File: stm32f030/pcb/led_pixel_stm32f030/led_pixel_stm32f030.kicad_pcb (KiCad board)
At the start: 2 copper layers, 50 x 50 mm, 52 parts, among them CON1 10PIN_JTAG_SWD, J1 Screw_Terminal_1x02, J2 CONN_01X10, J3 CONN_01X10, Q1 BC107, U1 STM32F030F4Px, U2 SN75176, U3 1117-3.3, U4 PT4115, U5 PT4115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

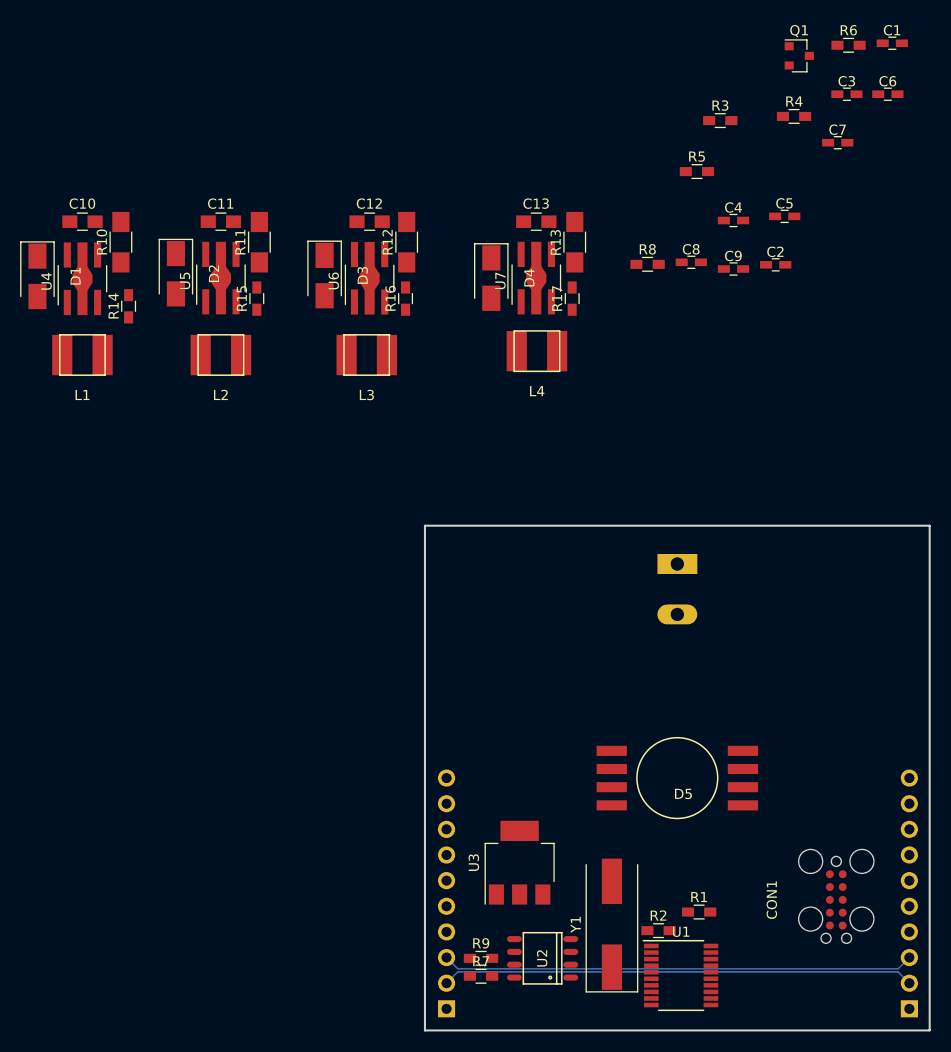
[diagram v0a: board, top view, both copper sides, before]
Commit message: made a first layout draft...
well okay, wouldn´t call it layout yet ;)

- next step make it look like a Layout XD
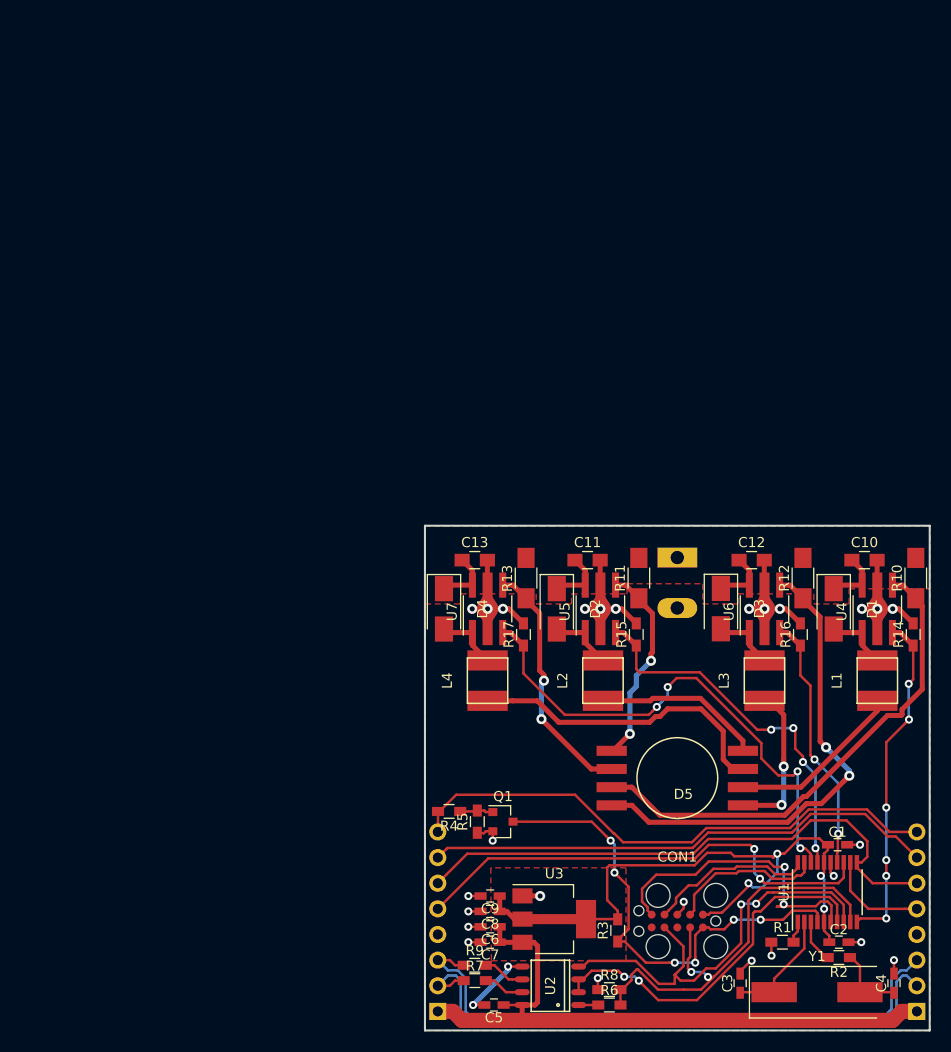
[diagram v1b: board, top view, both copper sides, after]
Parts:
- J2, J3: value CONN_01X10 -> CONN_01X08; footprint Pin_Headers:Pin_Header_Straight_1x10_Pitch2.54mm -> Pin_Headers:Pin_Header_Straight_1x08_Pitch2.54mm
- moved R6 98.0 mm to (143.3, 122.5)
- moved C6 91.4 mm to (131.5, 114.7), turned to 180 degrees
- moved C3 88.7 mm to (156.2, 120.3), turned to 90 degrees
- moved C7 86.4 mm to (131.5, 116.3), turned to 180 degrees
- moved D1 85.5 mm to (165.5, 83.2)
- moved R10 85.5 mm to (173.6, 80.2)
- moved U4 85.3 mm to (169.8, 83.2)
- moved L1 85.1 mm to (169.8, 90.3), turned to 90 degrees
- moved C10 84.4 mm to (168.5, 78.4)
- moved R14 84.2 mm to (173.4, 85.8)
- moved C5 83.3 mm to (131.8, 122.5), turned to 180 degrees
- moved Q1 81.3 mm to (132.7, 104.3)
- moved R3 80.9 mm to (144.1, 115.1), turned to 90 degrees
- moved C1 79.6 mm to (165.9, 106.6)
- moved C4 77.2 mm to (171.5, 120.3), turned to 90 degrees
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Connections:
- J2 pad 1: GND -> +5V
- J2 pad 5: /backplane/RESERVED -> /SPI_MOSI
- J2 pad 6: +5V -> /SPI_CLK
- J2 pad 7: /SPI_CLK -> /backplane/DAISY_R_TO_L
- J3 pad 1: GND -> +5V
- J3 pad 5: /backplane/RESERVED -> /SPI_MISO
- J3 pad 6: +5V -> /SPI_CLK
- J3 pad 7: /SPI_CLK -> /backplane/DAISY_R_TO_L
- U1 pad 14: /PWM_LED_W -> /PWM_LED_B
- U1 pad 18: /PWM_LED_B -> /PWM_LED_W
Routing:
- net GND: track 0.00 -> 81.9 mm, vias 0 -> 28
- net +3V3: track 0.00 -> 64.6 mm, vias 0 -> 4
- net +5V: track 0.00 -> 64.3 mm
- net /SPI_CLK: track 0.00 -> 55.9 mm
- net /RESET_IN: track 0.00 -> 54.4 mm
- net /PWM_LED_W: track 0.00 -> 51.1 mm, vias 0 -> 4
- net /backplane/DAISY_R_TO_L: track 0.00 -> 51.0 mm
- net /rgbw_led_driver/LED_R_A: track 0.00 -> 49.5 mm
- net /rgbw_led_driver/LED_B_A: track 0.00 -> 48.6 mm, vias 0 -> 2
- net /SPI_MOSI: track 0.00 -> 47.5 mm, vias 0 -> 2
- net /#RESET: track 0.00 -> 47.1 mm, vias 0 -> 6
- net /RS485_TX: track 0.00 -> 42.5 mm, vias 0 -> 2
- net /RS485_RX: track 0.00 -> 42.3 mm, vias 0 -> 2
- net /PWM_LED_G: track 0.00 -> 37.3 mm, vias 0 -> 4
- net /RS485_DE: track 0.00 -> 36.5 mm, vias 0 -> 2
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- added copper zone on F.Cu, net +3V3
- added copper zone on B.Cu, net GND
- added copper zone on F.Cu, net GND
- added copper zone on F.Cu, net VCC

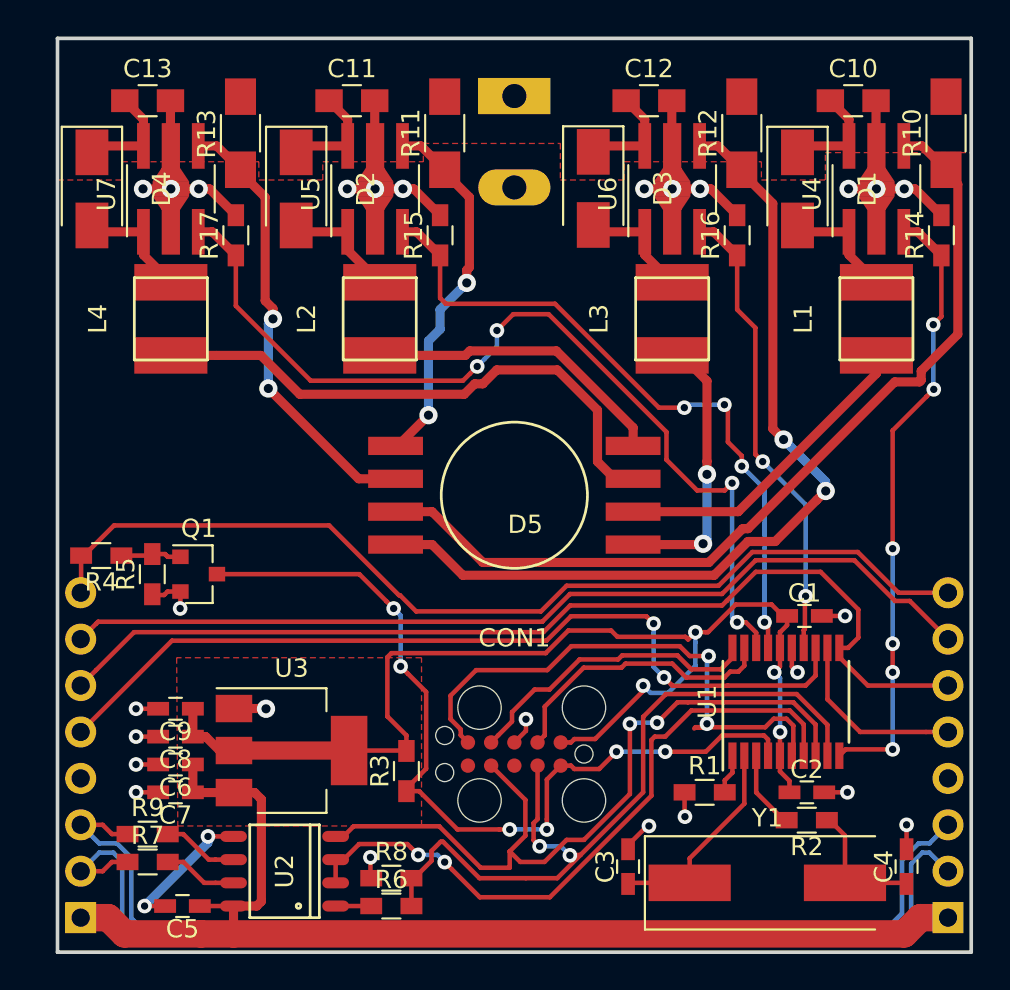
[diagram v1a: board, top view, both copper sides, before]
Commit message: added mounting holes
added a lot of capacitors (there was some room left ;) )

layout nearly finished
logos are missing ;)
not much work left I think
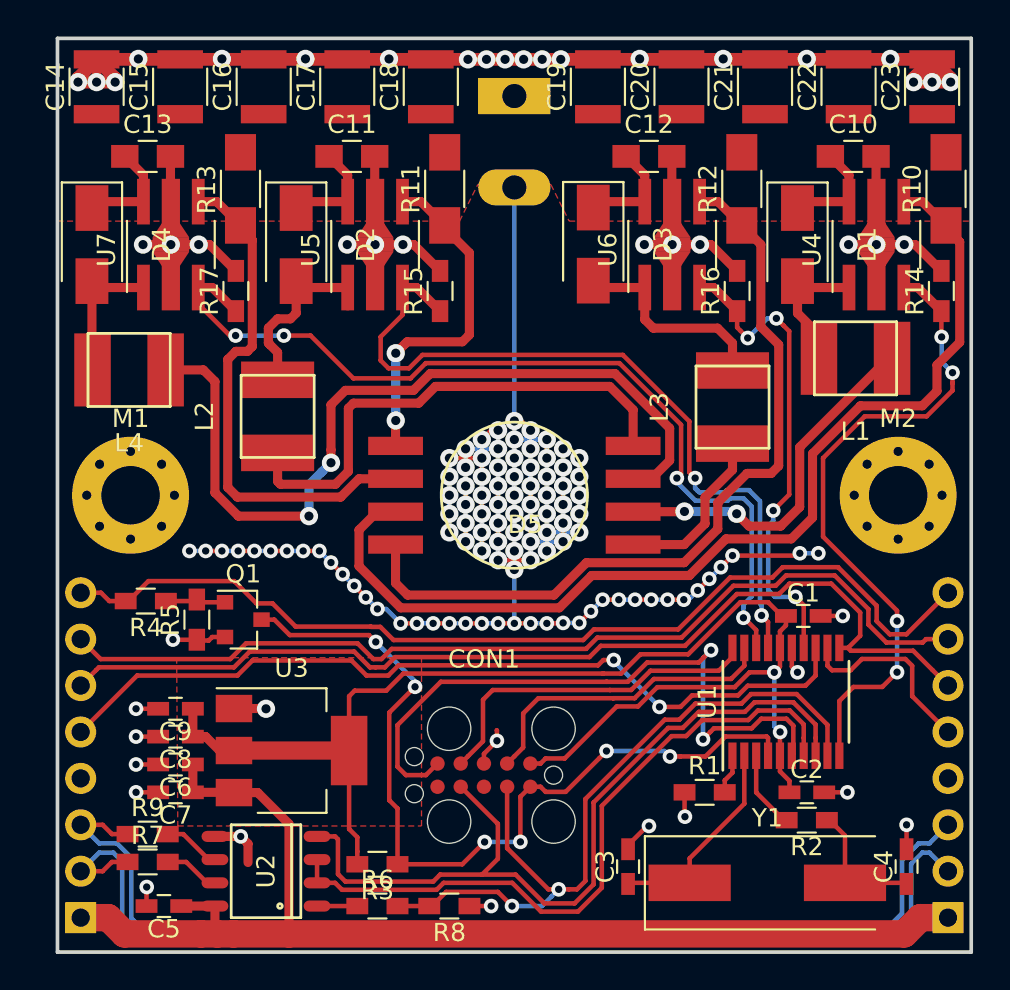
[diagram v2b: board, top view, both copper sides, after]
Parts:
- added C14: 10u 50V, Capacitors_SMD:C_1210, F.Cu at (127.1, 77.6)
- added C15: 10u 50V, Capacitors_SMD:C_1210, F.Cu at (131.7, 77.6)
- added C16: 10u 50V, Capacitors_SMD:C_1210, F.Cu at (136.3, 77.6)
- added C17: 10u 50V, Capacitors_SMD:C_1210, F.Cu at (140.9, 77.6)
- added C18: 10u 50V, Capacitors_SMD:C_1210, F.Cu at (145.4, 77.6)
- added C19: 10u 50V, Capacitors_SMD:C_1210, F.Cu at (154.6, 77.6)
- added C20: 10u 50V, Capacitors_SMD:C_1210, F.Cu at (159.1, 77.6)
- added C21: 10u 50V, Capacitors_SMD:C_1210, F.Cu at (163.7, 77.6)
- added C22: 10u 50V, Capacitors_SMD:C_1210, F.Cu at (168.3, 77.6)
- added C23: 10u 50V, Capacitors_SMD:C_1210, F.Cu at (172.9, 77.6)
- added M1: mounting hole, Mounting_Holes:MountingHole_3.2mm_M3_Pad_Via, F.Cu at (129.0, 100.0)
- added M2: mounting hole, Mounting_Holes:MountingHole_3.2mm_M3_Pad_Via, F.Cu at (171.0, 100.0)
- moved L2 7.73 mm to (137.0, 95.7)
- moved L3 5.85 mm to (161.9, 95.2)
- moved R3 5.34 mm to (142.5, 120.2), turned to 180 degrees
- moved L4 3.61 mm to (128.9, 93.1), turned to 180 degrees
- moved R8 3.52 mm to (146.4, 122.5), turned to 180 degrees
- moved Q1 3.48 mm to (135.2, 106.8)
- moved R4 3.48 mm to (129.8, 105.8)
- moved R5 3.48 mm to (132.6, 106.8)
- moved C10 3.05 mm to (168.5, 81.5)
- moved C11 3.05 mm to (141.1, 81.5)
- moved C12 3.05 mm to (157.4, 81.5)
- moved C13 3.05 mm to (129.9, 81.5)
- moved D1 3.05 mm to (165.5, 86.3)
- moved D2 3.05 mm to (138.1, 86.3)
- moved D3 3.05 mm to (154.3, 86.3)
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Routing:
- net GND: track 81.9 -> 262.3 mm, vias 28 -> 148
- net /rgbw_led_driver/LED_W_K: track 30.8 -> 47.0 mm, vias 0 -> 2
- net /rgbw_led_driver/LED_G_K: track 16.7 -> 27.8 mm
- net /rgbw_led_driver/LED_R_A: track 49.5 -> 57.6 mm
- net +3V3: track 64.6 -> 71.8 mm, vias 4 -> 2
- net /rgbw_led_driver/LED_B_K: track 15.5 -> 9.41 mm, vias 2 -> 0
- net Net-(D3-Pad2): track 6.36 -> 12.5 mm
- net /TESTMODE: track 30.4 -> 36.1 mm
- net /PWM_LED_G: track 37.3 -> 41.9 mm, vias 4 -> 2
- net /rgbw_led_driver/LED_B_A: track 48.6 -> 44.1 mm, vias 2 -> 0
- net Net-(D2-Pad2): track 6.45 -> 10.6 mm
- net /rgbw_led_driver/LED_W_A: track 25.7 -> 29.2 mm, vias 2 -> 0
- net /RS485_TX: track 42.5 -> 45.6 mm, vias 2 -> 0
- net /SWCLK: track 16.6 -> 19.1 mm
- net /PWM_LED_R: track 33.8 -> 36.2 mm, vias 6 -> 4
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
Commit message: finished layout for stm32f0 version
the silkscreen has to be fixed...
documentation and production data has to be generated
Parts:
- added G***: LOGO, proz_logo:Shimatta_SolderMask, B.Cu at (161.5, 120.8)
- added REF**: KiCAD Logo, Symbols:Symbol_KiCAD-Logo_CopperAndSilkScreenTop, B.Cu at (136.8, 115.2)
- added REF***: ESD-Logo_8.9x8mm_SilkScreen, Symbols:ESD-Logo_8.9x8mm_SilkScreen, B.Cu at (169.8, 81.2)
- added REF***: WEEE-Logo_4.2x6mm_SilkScreen, Symbols:WEEE-Logo_4.2x6mm_SilkScreen, B.Cu at (129.2, 81.7)
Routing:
- net /#RESET: track 46.7 -> 52.9 mm
- net GND: track 262.3 -> 264.3 mm, vias 148 -> 149
- net /RS485_TX: track 45.6 -> 47.4 mm
- net /RS485_RX: track 41.2 -> 39.8 mm
- net /rgbw_led_driver/LED_B_A: track 44.1 -> 43.2 mm
- net /rgbw_led_driver/LED_R_A: track 57.6 -> 58.4 mm
- net /rgbw_led_driver/LED_R_K: track 20.2 -> 21.0 mm
- net /backplane/DAISY_R_TO_L: track 52.6 -> 51.9 mm
- net /SPI_CLK: track 55.3 -> 54.6 mm
- net /RS485_DE: track 38.1 -> 37.5 mm
- net /PWM_LED_R: track 36.2 -> 36.7 mm
- net /PWM_LED_W: track 49.6 -> 50.1 mm
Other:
- board text added: "05/2017"

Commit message: hopefully finished everything
generated documentation and gerber files
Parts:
- moved G*** 33.5 mm to (150.0, 89.3)
- moved REF** 0.89 mm to (136.8, 116.1)
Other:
- board text added: "+5V"
- board text added: "GND"
- board text added: "RS485_N"
- board text added: "RS485_P"
- board text added: "daisy clk"
- board text added: "daisy in"
- board text added: "daisy out"
- board text added: "daisy rtn"
- board text added: "reset"

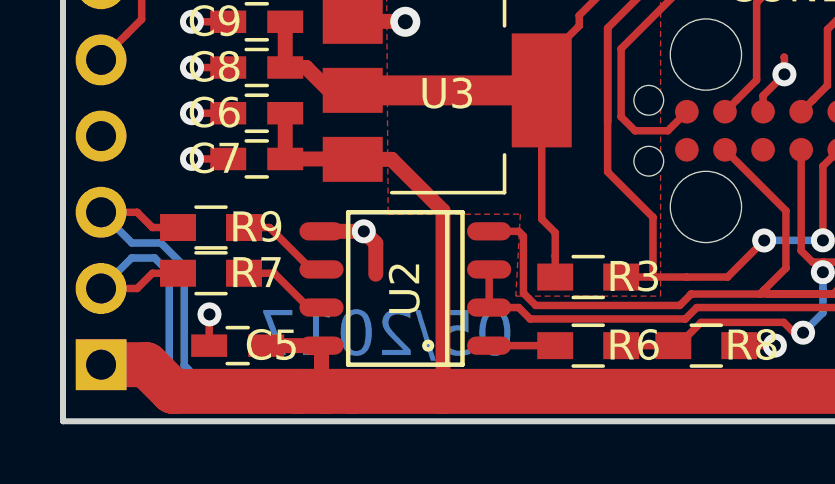
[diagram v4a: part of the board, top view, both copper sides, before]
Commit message: added pcb number and revision
re generated all docu and gerber data
- ordered this one as rev 1.0
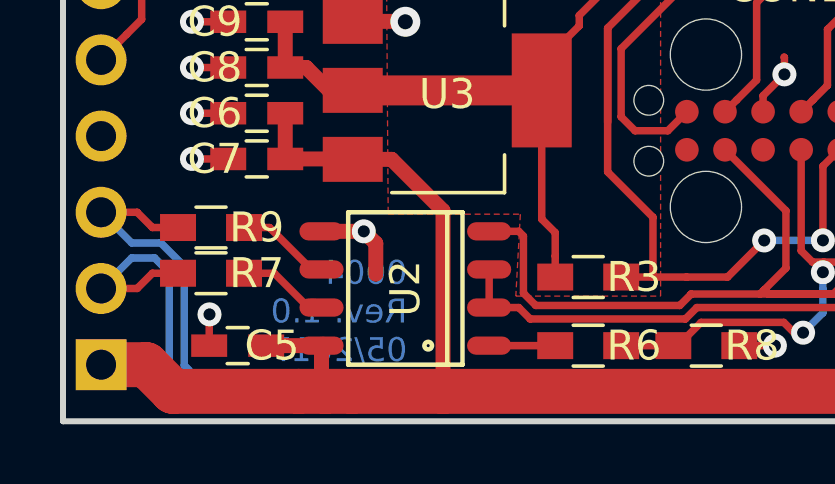
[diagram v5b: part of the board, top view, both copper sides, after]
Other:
- board text added: "0004 Rev: 1.0 05/2017"
- board text removed: "05/2017"
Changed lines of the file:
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@@
-(kicad_pcb (version 20170123) (host pcbnew "(2017-05-08 revision d4e41c4f9)-makepkg")
+(kicad_pcb (version 20170123) (host pcbnew "(2017-05-12 revision b823d0b78)-makepkg")
   (general
     (links 163)
@@
   )
   (page A4)
+  (title_block
+    (title led_pixel_stm32f030)
+    (date 2017-05-13)
+    (rev 1.0)
+    (company shimatta)
+  )
   (layers
     (0 F.Cu signal)
@@
     (visible_elements 7FFFFFFF)
     (pcbplotparams
-      (layerselection 0x000fc_ffffffff)
+      (layerselection 0x010fc_ffffffff)
       (usegerberextensions true)
       (excludeedgelayer false)
@@
       (outputformat 4)
       (mirror false)
-      (drillshape 2)
+      (drillshape 0)
       (scaleselection 1)
       (outputdirectory doc/))
@@
     (effects (font (size 1.5 1.5) (thickness 0.3)) (justify mirror))
   )
-  (gr_text 05/2017 (at 135.776 122.098) (layer B.Cu)
-    (effects (font (size 1.5 1.5) (thickness 0.3)) (justify mirror))
+  (gr_text "0004\nRev: 1.0\n05/2017" (at 136.4745 121.336) (layer B.Cu)
+    (effects (font (size 0.8 0.8) (thickness 0.2)) (justify left mirror))
   )
   (gr_line (start 125 125) (end 125 75) (layer Edge.Cuts) (width 0.2))

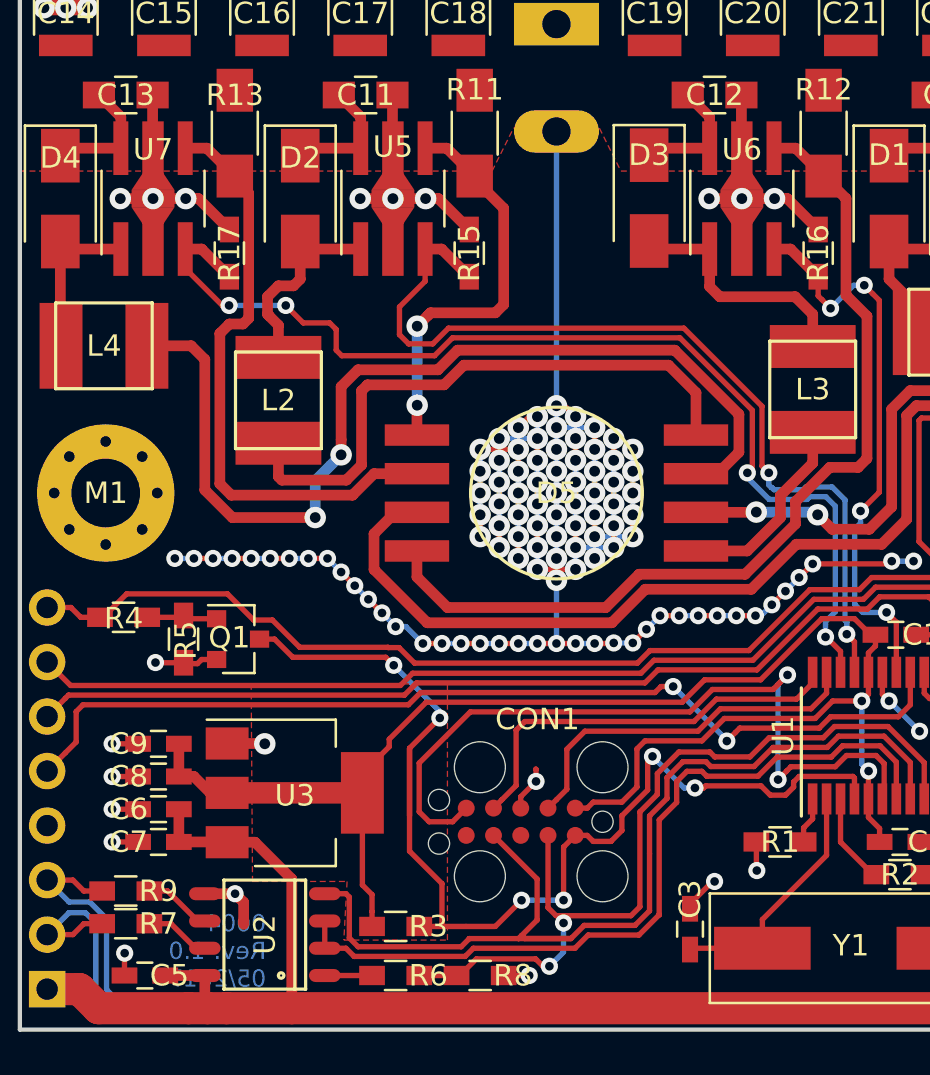
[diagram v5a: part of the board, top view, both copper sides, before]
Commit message: updraded to revision V1.1
Now the cooling pad of the LED is isolated from the ground plane.
Unfortunately there will be less cooling than before, but the LEDs to use have a stupid connection...
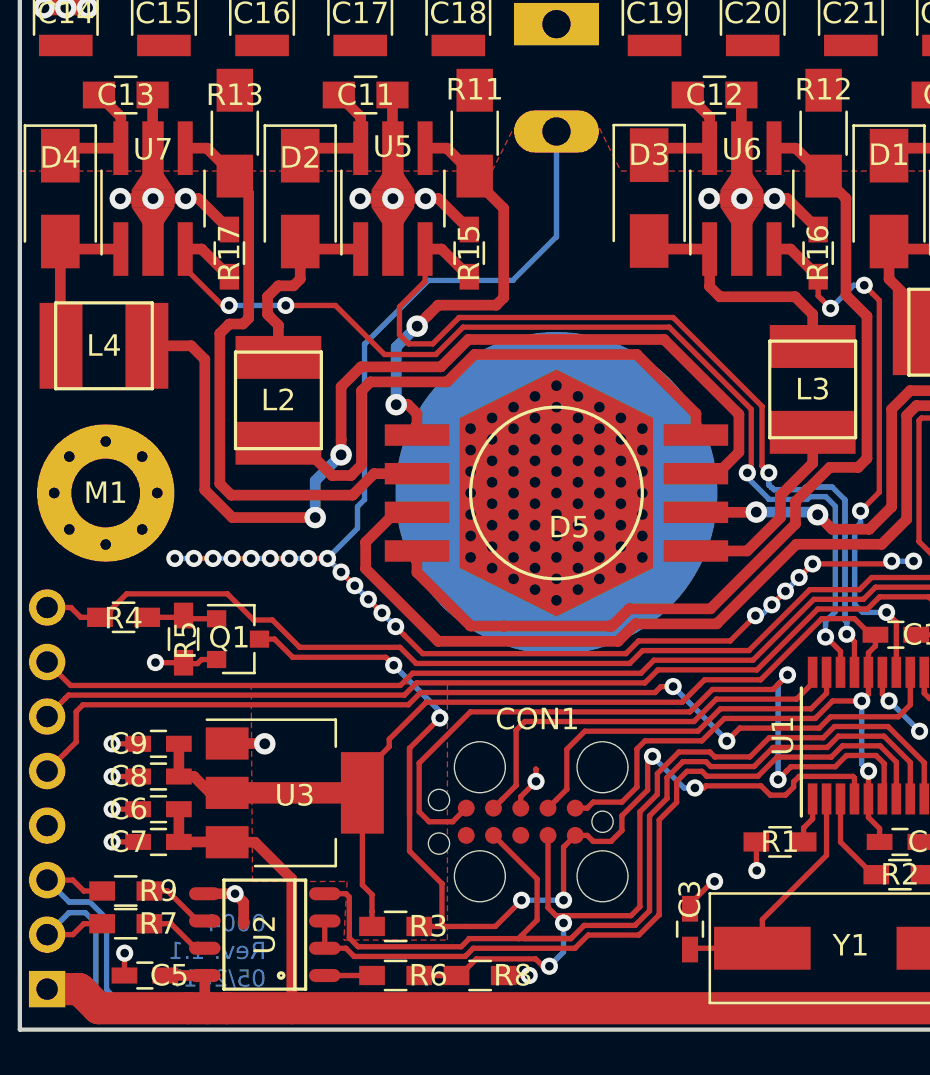
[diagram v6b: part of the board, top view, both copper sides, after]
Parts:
- D5: footprint proz_led:LED_SMD_RGBW_4W -> proz_led:LED_SMD_RGBW_4W_ISOLATED
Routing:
- net GND: track 264.3 -> 208.9 mm, vias 149 -> 70
- net /rgbw_led_driver/LED_G_K: track 27.8 -> 26.6 mm
- net /rgbw_led_driver/LED_R_A: track 58.4 -> 59.6 mm
- net /rgbw_led_driver/LED_G_A: track 18.9 -> 19.9 mm
- net /rgbw_led_driver/LED_B_A: track 43.2 -> 43.8 mm
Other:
- board text added: "0004 Rev: 1.1 05/2017"
- board text removed: "0004 Rev: 1.0 05/2017"
